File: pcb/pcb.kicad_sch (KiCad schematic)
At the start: 247 parts, among them J1 USB_C_Receptacle_USB2.0, J2 AVR-ISP-6, SW1 1U, SW10 1U, SW100 2U, SW101 1.25U CTRL, SW102 1.25U GUI, SW103 1.25U ALT, SW104 6.25u SPACE, SW105 1U ALT, SW106 1U GUI, SW107 1U CTRL, SW108 1U, SW109 1U, SW11 1U, SW110 1U, SW111 1U, SW112 1U, SW113 1U, SW114 1.5U CTRL, SW115 1U GUI, SW116 1.5U ALT, SW117 7U SPACE, SW118 1.5U ALT, SW119 1.5U CTRL, SW12 1U, SW120 1.5U GUI, SW121 6U SPACE, SW122 SW_Push, SW123 SW_Push, SW13 1U, SW14 1U, SW15 1U, SW16 1U, SW17 1U, SW18 1U, SW19 1U, SW2 1U, SW20 1U, SW21 1U, SW22 1U, SW23 1U, SW24 1U, SW25 1U, SW26 1U, SW27 1U, SW28 1U, SW29 1U, SW3 1U, SW30 1U, SW31 1U, SW32 1U, SW33 1U, SW34 1U, SW35 1U, SW36 1U, SW37 1U, SW38 1U, SW39 1U, SW4 1U, SW40 1U, SW41 2U, SW42 1U, SW43 1.5U, SW44 1U, SW45 1U, SW46 1U, SW47 1U, SW48 1U, SW49 1U, SW5 1U, SW50 1U, SW51 1U, SW52 1U, SW53 1U, SW54 1U, SW55 1.5U, SW56 1U, SW57 1U, SW58 1U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

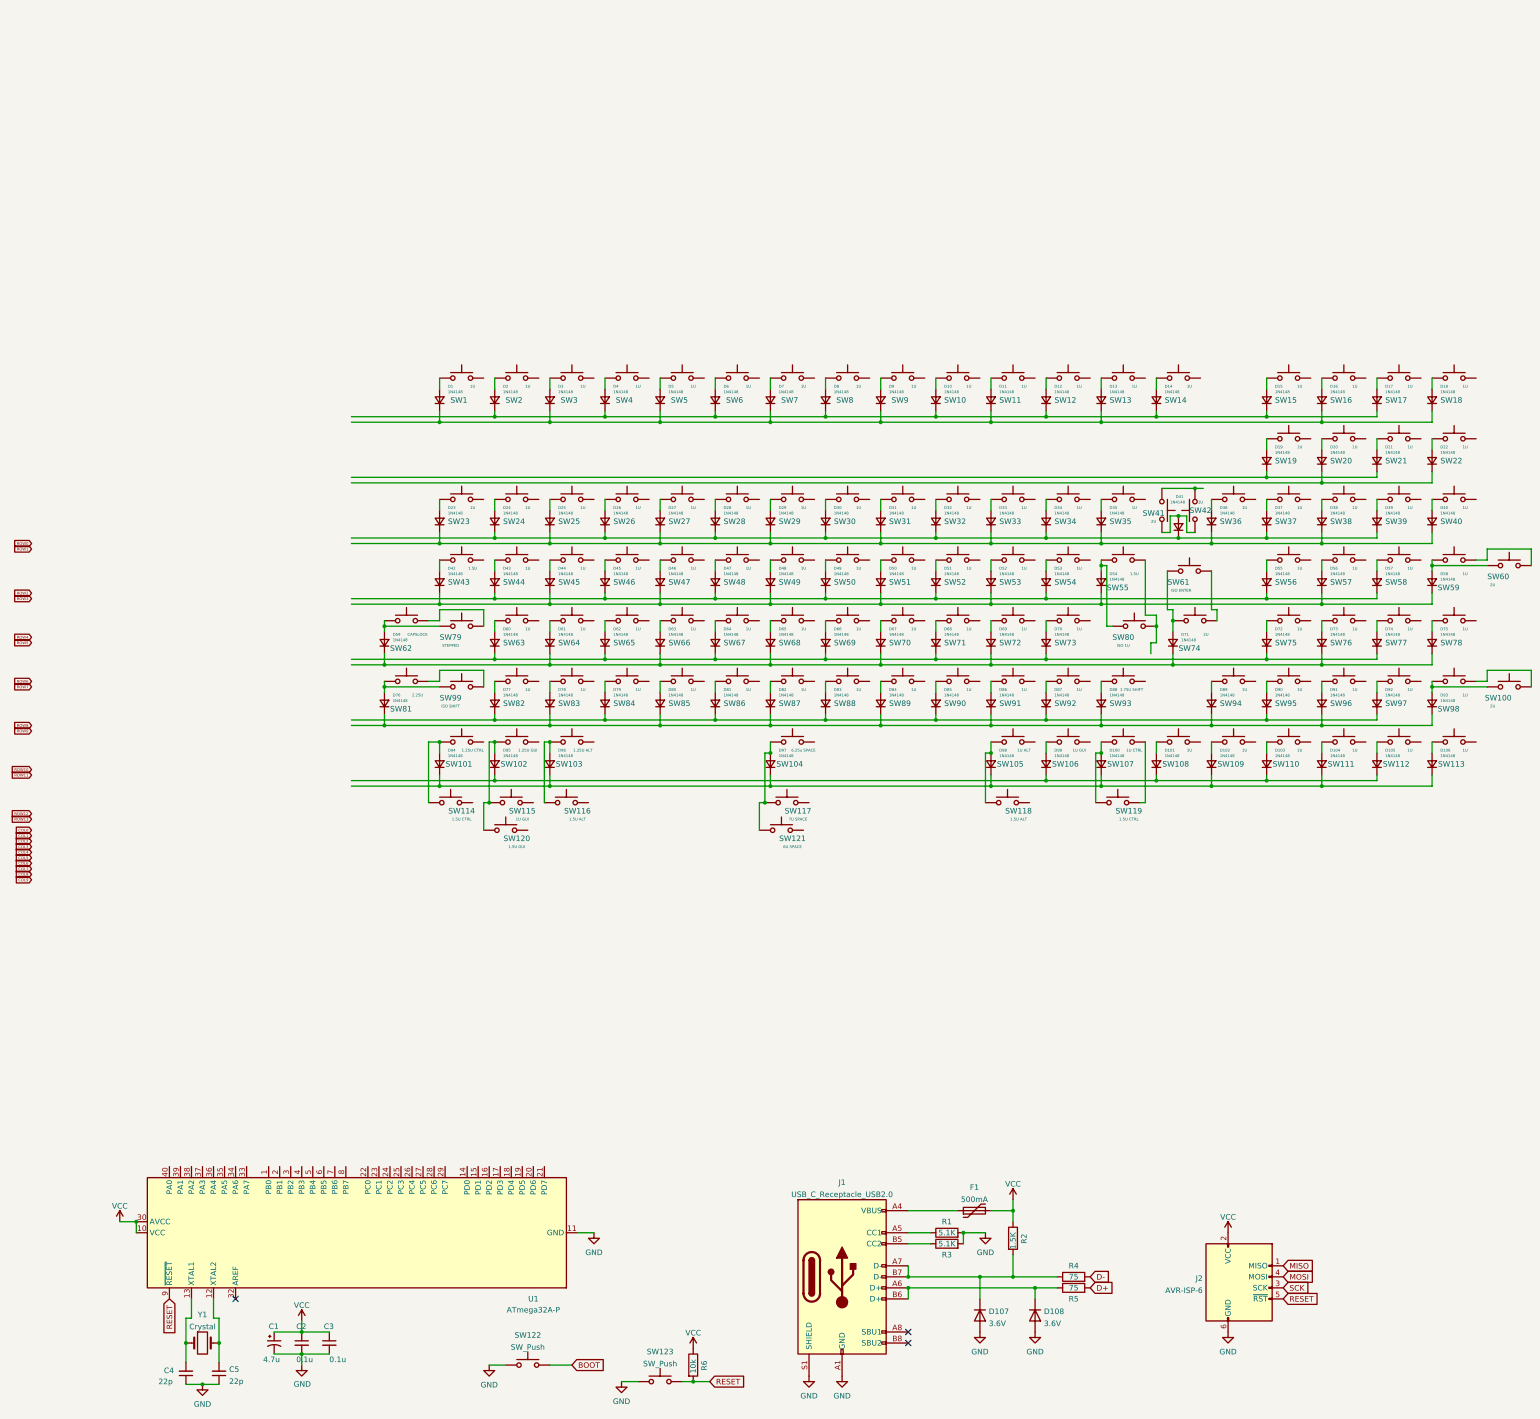
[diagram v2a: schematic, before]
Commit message: Main wiring schematic finally done, keys organized on PCB
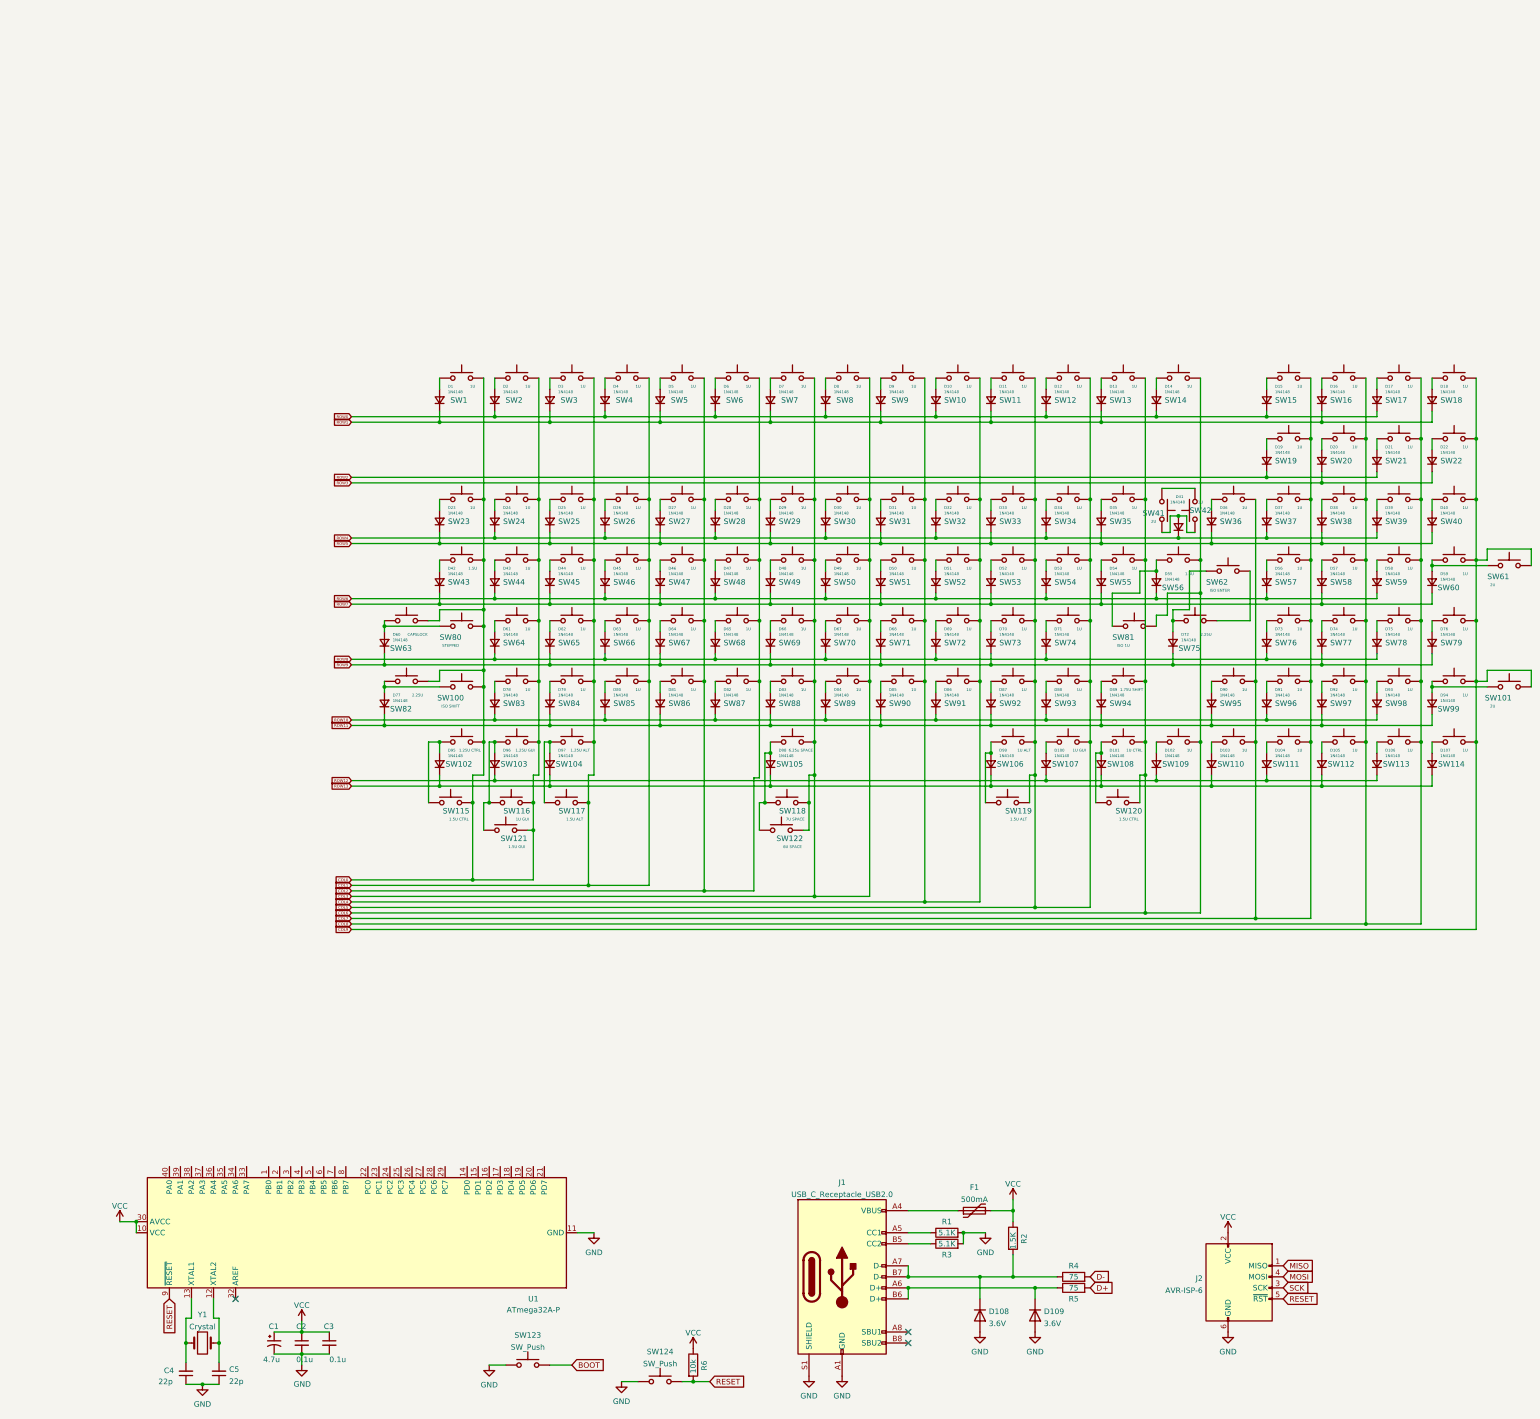
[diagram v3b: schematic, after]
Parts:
- added D54: 1N4148, Diode_THT:D_DO-35_SOD27_P7.62mm_Horizontal, symbol Device:D_Small
- added SW55: 1U, MX_Only:MXOnly-1U-NoLED, symbol Switch:SW_Push
- SW101: renamed from SW100; footprint MX_Only:MXOnly-2U-NoLED -> MX_Only:MXOnly-2U-VerticalStabilizers-NoLED
- SW61: renamed from SW60; footprint MX_Only:MXOnly-2U-NoLED -> MX_Only:MXOnly-2U-VerticalStabilizers-NoLED
- SW75: renamed from SW74; value 2U -> 2.25U; footprint MX_Only:MXOnly-2U-NoLED -> MX_Only:MXOnly-2.25U-NoLED
- renumbered D99 to D100, D100 to D101, D101 to D102, D102 to D103, D103 to D104, D104 to D105, D105 to D106, D106 to D107, D107 to D108, D108 to D109, D54 to D55, D55 to D56, D56 to D57, D57 to D58, D58 to D59, D59 to D60, D60 to D61, D61 to D62, D62 to D63, D63 to D64, D64 to D65, D65 to D66, D66 to D67, D67 to D68, D68 to D69, D69 to D70, D70 to D71, D71 to D72, D72 to D73, D73 to D74, D74 to D75, D75 to D76, D76 to D77, D77 to D78, D78 to D79, D79 to D80, D80 to D81, D81 to D82, D82 to D83, D83 to D84, D84 to D85, D85 to D86, D86 to D87, D87 to D88, D88 to D89, D89 to D90, D90 to D91, D91 to D92, D92 to D93, D93 to D94, D94 to D95, D95 to D96, D96 to D97, D97 to D98, D98 to D99, SW99 to SW100, SW101 to SW102, SW102 to SW103, SW103 to SW104, SW104 to SW105, SW105 to SW106, SW106 to SW107, SW107 to SW108, SW108 to SW109, SW109 to SW110, SW110 to SW111, SW111 to SW112, SW112 to SW113, SW113 to SW114, SW114 to SW115, SW115 to SW116, SW116 to SW117, SW117 to SW118, SW118 to SW119, SW119 to SW120, SW120 to SW121, SW121 to SW122, SW122 to SW123, SW123 to SW124, SW55 to SW56, SW56 to SW57, SW57 to SW58, SW58 to SW59, SW59 to SW60, SW61 to SW62, SW62 to SW63, SW63 to SW64, SW64 to SW65, SW65 to SW66, SW66 to SW67, SW67 to SW68, SW68 to SW69, SW69 to SW70, SW70 to SW71, SW71 to SW72, SW72 to SW73, SW73 to SW74, SW75 to SW76, SW76 to SW77, SW77 to SW78, SW78 to SW79, SW79 to SW80, SW80 to SW81, SW81 to SW82, SW82 to SW83, SW83 to SW84, SW84 to SW85, SW85 to SW86, SW86 to SW87, SW87 to SW88, SW88 to SW89, SW89 to SW90, SW90 to SW91, SW91 to SW92, SW92 to SW93, SW93 to SW94, SW94 to SW95, SW95 to SW96, SW96 to SW97, SW97 to SW98, SW98 to SW99
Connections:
- net COL0: now also SW1.2, SW100.2, SW102.2, SW103.2, SW115.2, SW116.2, SW121.2, SW2.2, SW23.2, SW24.2, SW43.2, SW44.2, SW63.2, SW64.2, SW80.2, SW82.2, SW83.2
- net COL1: now also SW104.2, SW117.2, SW25.2, SW26.2, SW3.2, SW4.2, SW45.2, SW46.2, SW65.2, SW66.2, SW84.2, SW85.2
- net COL2: now also SW27.2, SW28.2, SW47.2, SW48.2, SW5.2, SW6.2, SW67.2, SW68.2, SW86.2, SW87.2
- net COL3: now also SW105.2, SW118.2, SW122.2, SW29.2, SW30.2, SW49.2, SW50.2, SW69.2, SW7.2, SW70.2, SW8.2, SW88.2, SW89.2
- net COL4: now also SW10.2, SW31.2, SW32.2, SW51.2, SW52.2, SW71.2, SW72.2, SW9.2, SW90.2, SW91.2
- net COL5: now also SW106.2, SW107.2, SW11.2, SW119.2, SW12.2, SW33.2, SW34.2, SW53.2, SW54.2, SW73.2, SW74.2, SW92.2, SW93.2
- net COL6: now also SW108.2, SW109.2, SW120.2, SW13.2, SW14.2, SW35.2, SW56.2, SW81.2, SW94.2, SW55.2
- net COL7: now also SW110.2, SW111.2, SW15.2, SW19.2, SW36.2, SW37.2, SW57.2, SW76.2, SW95.2, SW96.2
- net COL8: now also SW112.2, SW113.2, SW16.2, SW17.2, SW20.2, SW21.2, SW38.2, SW39.2, SW58.2, SW59.2, SW77.2, SW78.2, SW97.2, SW98.2
- net COL9: now also SW101.2, SW114.2, SW18.2, SW22.2, SW40.2, SW60.2, SW61.2, SW79.2, SW99.2
- net ROW0: now also D10.1 (K), D12.1 (K), D14.1 (K), D15.1 (K), D17.1 (K), D2.1 (K), D4.1 (K), D6.1 (K), D8.1 (K)
- net ROW1: now also D1.1 (K), D11.1 (K), D13.1 (K), D16.1 (K), D18.1 (K), D3.1 (K), D5.1 (K), D7.1 (K), D9.1 (K)
- net ROW10: now also D78.1 (K), D80.1 (K), D82.1 (K), D84.1 (K), D86.1 (K), D88.1 (K), D91.1 (K), D93.1 (K)
- net ROW11: now also D77.1 (K), D79.1 (K), D81.1 (K), D83.1 (K), D85.1 (K), D87.1 (K), D89.1 (K), D90.1 (K), D92.1 (K), D94.1 (K)
- net ROW12: now also D100.1 (K), D102.1 (K), D104.1 (K), D106.1 (K), D96.1 (K)
- net ROW13: now also D101.1 (K), D103.1 (K), D105.1 (K), D107.1 (K), D95.1 (K), D97.1 (K), D98.1 (K), D99.1 (K)
- net ROW2: now also D19.1 (K), D21.1 (K)
- net ROW3: now also D20.1 (K), D22.1 (K)
- net ROW4: now also D24.1 (K), D26.1 (K), D28.1 (K), D30.1 (K), D32.1 (K), D34.1 (K), D37.1 (K), D39.1 (K), D41.1 (K)
- net ROW5: now also D23.1 (K), D25.1 (K), D27.1 (K), D29.1 (K), D31.1 (K), D33.1 (K), D35.1 (K), D36.1 (K), D38.1 (K), D40.1 (K)
- net ROW6: now also D43.1 (K), D45.1 (K), D47.1 (K), D49.1 (K), D51.1 (K), D53.1 (K), D55.1 (K), D56.1 (K), D58.1 (K)
- net ROW7: now also D42.1 (K), D44.1 (K), D46.1 (K), D48.1 (K), D50.1 (K), D52.1 (K), D57.1 (K), D59.1 (K), D54.1 (K)
- net ROW8: now also D61.1 (K), D63.1 (K), D65.1 (K), D67.1 (K), D69.1 (K), D71.1 (K), D73.1 (K), D75.1 (K)
- net ROW9: now also D60.1 (K), D62.1 (K), D64.1 (K), D66.1 (K), D68.1 (K), D70.1 (K), D72.1 (K), D74.1 (K), D76.1 (K)
- new net: D54.2 (A), SW55.1
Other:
- moved on the sheet: D55, SW56, SW62

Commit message: PCB components placed
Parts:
- removed D41: 1N4148, Diode_THT:D_DO-35_SOD27_P7.62mm_Horizontal, symbol Device:D_Small
- removed SW41: 2U, MX_Only:MXOnly-2U-NoLED, symbol Switch:SW_Push
- removed SW42: 1U, MX_Only:MXOnly-1U-NoLED, symbol Switch:SW_Push
- added D36: 1N4148, Diode_THT:D_DO-35_SOD27_P7.62mm_Horizontal, symbol Device:D_Small
- added SW23: 1U, MX_Only:MXOnly-1U-NoLED, symbol Switch:SW_Push
- added SW37: 2U, MX_Only:MXOnly-2U-NoLED, symbol Switch:SW_Push
- renumbered D36 to D37, D37 to D38, D38 to D39, D39 to D40, D40 to D41, SW23 to SW24, SW24 to SW25, SW25 to SW26, SW26 to SW27, SW27 to SW28, SW28 to SW29, SW29 to SW30, SW30 to SW31, SW31 to SW32, SW32 to SW33, SW33 to SW34, SW34 to SW35, SW35 to SW36, SW36 to SW38, SW37 to SW39, SW38 to SW40, SW39 to SW41, SW40 to SW42
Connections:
- net COL6: now also SW62.2, SW75.2, SW23.2, SW37.2
- net ROW4: now also D36.1 (K)
- new net: D36.2 (A), SW23.1, SW37.1

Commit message: God help me with these diodes
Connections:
- net ROW13 is gone; now on net ROW12: D101.1 (K), D103.1 (K), D105.1 (K), D107.1 (K), D95.1 (K), D97.1 (K), D98.1 (K), D99.1 (K)
- net COL0: now also U1.28 (PC6)
- net COL1: now also U1.29 (PC7)
- net COL2: now also U1.33 (PA7)
- net COL3: now also U1.34 (PA6)
- net COL4: now also U1.35 (PA5)
- net COL5: now also U1.36 (PA4)
- net COL6: now also U1.37 (PA3)
- net COL7: now also U1.38 (PA2)
- net COL8: now also U1.39 (PA1)
- net COL9: now also U1.40 (PA0)
- net D+: now also U1.26 (PC4)
- net D-: now also U1.27 (PC5)
- net MISO: now also U1.15 (PD1)
- net MOSI: now also U1.16 (PD2)
- net ROW10: now also D77.1 (K), D79.1 (K), D81.1 (K), D83.1 (K), D85.1 (K), D87.1 (K), D89.1 (K), D90.1 (K), D92.1 (K), D94.1 (K); no longer D78.1 (K), D80.1 (K), D82.1 (K), D84.1 (K), D86.1 (K), D88.1 (K), D91.1 (K), D93.1 (K)
- net ROW11: now also D100.1 (K), D102.1 (K), D104.1 (K), D106.1 (K), D96.1 (K); no longer D77.1 (K), D79.1 (K), D81.1 (K), D83.1 (K), D85.1 (K), D87.1 (K), D89.1 (K), D90.1 (K), D92.1 (K), D94.1 (K)
- net ROW12: no longer D100.1 (K), D102.1 (K), D104.1 (K), D106.1 (K), D96.1 (K)
- net ROW2: now also D20.1 (K), D22.1 (K)
- net ROW3: now also D24.1 (K), D26.1 (K), D28.1 (K), D30.1 (K), D32.1 (K), D34.1 (K), D36.1 (K), D38.1 (K), D40.1 (K); no longer D20.1 (K), D22.1 (K)
- net ROW4: now also D23.1 (K), D25.1 (K), D27.1 (K), D29.1 (K), D31.1 (K), D33.1 (K), D35.1 (K), D37.1 (K), D39.1 (K), D41.1 (K); no longer D24.1 (K), D26.1 (K), D28.1 (K), D30.1 (K), D32.1 (K), D34.1 (K), D36.1 (K), D38.1 (K), D40.1 (K)
- net ROW5: now also D43.1 (K), D45.1 (K), D47.1 (K), D49.1 (K), D51.1 (K), D53.1 (K), D55.1 (K), D56.1 (K), D58.1 (K); no longer D23.1 (K), D25.1 (K), D27.1 (K), D29.1 (K), D31.1 (K), D33.1 (K), D35.1 (K), D37.1 (K), D39.1 (K), D41.1 (K)
- net ROW6: now also D42.1 (K), D44.1 (K), D46.1 (K), D48.1 (K), D50.1 (K), D52.1 (K), D54.1 (K), D57.1 (K), D59.1 (K); no longer D43.1 (K), D45.1 (K), D47.1 (K), D49.1 (K), D51.1 (K), D53.1 (K), D55.1 (K), D56.1 (K), D58.1 (K)
- net ROW7: now also D61.1 (K), D63.1 (K), D65.1 (K), D67.1 (K), D69.1 (K), D71.1 (K), D73.1 (K), D75.1 (K); no longer D42.1 (K), D44.1 (K), D46.1 (K), D48.1 (K), D50.1 (K), D52.1 (K), D54.1 (K), D57.1 (K), D59.1 (K)
- net ROW8: now also D60.1 (K), D62.1 (K), D64.1 (K), D66.1 (K), D68.1 (K), D70.1 (K), D72.1 (K), D74.1 (K), D76.1 (K); no longer D61.1 (K), D63.1 (K), D65.1 (K), D67.1 (K), D69.1 (K), D71.1 (K), D73.1 (K), D75.1 (K)
- net ROW9: now also D78.1 (K), D80.1 (K), D82.1 (K), D84.1 (K), D86.1 (K), D88.1 (K), D91.1 (K), D93.1 (K); no longer D60.1 (K), D62.1 (K), D64.1 (K), D66.1 (K), D68.1 (K), D70.1 (K), D72.1 (K), D74.1 (K), D76.1 (K)
- net SCK: now also U1.14 (PD0)

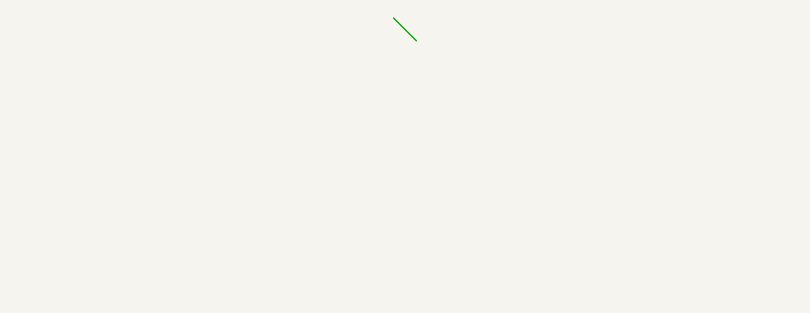
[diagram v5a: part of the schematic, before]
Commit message: Started routing of rows
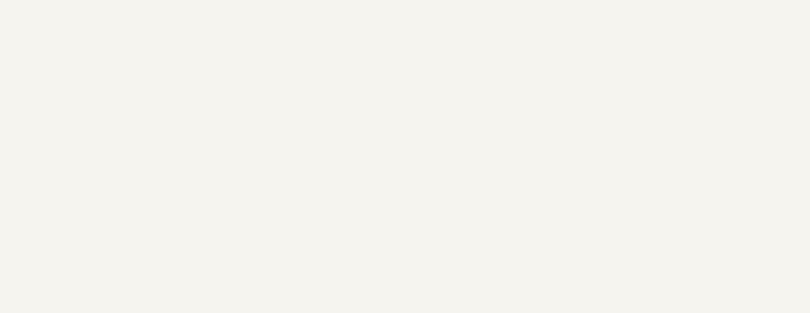
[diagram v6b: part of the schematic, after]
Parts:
- SW101, SW61: footprint MX_Only:MXOnly-2U-VerticalStabilizers-NoLED -> MX_Only:MXOnly-2U-ReversedVerticalStabilizers-NoLED
- SW105: footprint MX_Only:MXOnly-6.25U-NoLED -> MX_Only:MXOnly-6.25U-ReversedStabilizers-NoLED
- SW118: footprint MX_Only:MXOnly-7U-NoLED -> MX_Only:MXOnly-7U-ReversedStabilizers-NoLED
- SW122: footprint MX_Only:MXOnly-6U-NoLED -> MX_Only:MXOnly-6U-ReversedStabilizers-NoLED
- SW62: footprint MX_Only:MXOnly-ISO-NoLED -> MX_Only:MXOnly-ISO-ReversedStabilizers-NoLED
- SW75, SW82: footprint MX_Only:MXOnly-2.25U-NoLED -> MX_Only:MXOnly-2.25U-ReversedStabilizers-NoLED
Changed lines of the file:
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@@
   (no_connect (at 45.72 255.27))
   (no_connect (at 200.66 262.89))
-  (bus_entry (at 207.645 -41.91) (size 2.54 2.54)
-    (stroke (width 0) (type default) (color 0 0 0 0))
-  )
   (wire (pts (xy 232.41 52.07) (xy 257.81 52.07))
     (stroke (width 0) (type default) (color 0 0 0 0))
@@
       (effects (font (size 0.635 0.635)))
     )
-    (property "Footprint" "MX_Only:MXOnly-2U-VerticalStabilizers-NoLED" (id 2) (at 339.09 109.22 0)
+    (property "Footprint" "MX_Only:MXOnly-2U-ReversedVerticalStabilizers-NoLED" (id 2) (at 339.09 109.22 0)
       (effects (font (size 1.27 1.27)) hide)
     )
@@
       (effects (font (size 0.635 0.635)))
     )
-    (property "Footprint" "MX_Only:MXOnly-ISO-NoLED" (id 2) (at 274.32 82.55 0)
+    (property "Footprint" "MX_Only:MXOnly-ISO-ReversedStabilizers-NoLED" (id 2) (at 274.32 82.55 0)
       (effects (font (size 1.27 1.27)) hide)
     )
@@
       (effects (font (size 0.635 0.635)))
     )
-    (property "Footprint" "MX_Only:MXOnly-2.25U-NoLED" (id 2) (at 266.7 93.98 0)
+    (property "Footprint" "MX_Only:MXOnly-2.25U-ReversedStabilizers-NoLED" (id 2) (at 266.7 93.98 0)
       (effects (font (size 1.27 1.27)) hide)
     )
@@
       (effects (font (size 0.635 0.635)))
     )
-    (property "Footprint" "MX_Only:MXOnly-2.25U-NoLED" (id 2) (at 85.09 107.95 0)
+    (property "Footprint" "MX_Only:MXOnly-2.25U-ReversedStabilizers-NoLED" (id 2) (at 85.09 107.95 0)
       (effects (font (size 1.27 1.27)) hide)
     )
@@
       (effects (font (size 0.635 0.635)))
     )
-    (property "Footprint" "MX_Only:MXOnly-2U-VerticalStabilizers-NoLED" (id 2) (at 339.09 81.28 0)
+    (property "Footprint" "MX_Only:MXOnly-2U-ReversedVerticalStabilizers-NoLED" (id 2) (at 339.09 81.28 0)
       (effects (font (size 1.27 1.27)) hide)
     )
@@
       (effects (font (size 0.635 0.635)))
     )
-    (property "Footprint" "MX_Only:MXOnly-6U-NoLED" (id 2) (at 171.45 142.24 0)
+    (property "Footprint" "MX_Only:MXOnly-6U-ReversedStabilizers-NoLED" (id 2) (at 171.45 142.24 0)
       (effects (font (size 1.27 1.27)) hide)
     )
@@
       (effects (font (size 0.635 0.635)))
     )
-    (property "Footprint" "MX_Only:MXOnly-6.25U-NoLED" (id 2) (at 173.99 121.92 0)
+    (property "Footprint" "MX_Only:MXOnly-6.25U-ReversedStabilizers-NoLED" (id 2) (at 173.99 121.92 0)
       (effects (font (size 1.27 1.27)) hide)
     )
@@
       (effects (font (size 0.635 0.635)))
     )
-    (property "Footprint" "MX_Only:MXOnly-7U-NoLED" (id 2) (at 172.72 135.89 0)
+    (property "Footprint" "MX_Only:MXOnly-7U-ReversedStabilizers-NoLED" (id 2) (at 172.72 135.89 0)
       (effects (font (size 1.27 1.27)) hide)
     )
@@
     )
     (path "/2b191c2c-1167-46dd-8fa0-bd72c7ca26a5"
-      (reference "SW61") (unit 1) (value "2U") (footprint "MX_Only:MXOnly-2U-VerticalStabilizers-NoLED")
+      (reference "SW61") (unit 1) (value "2U") (footprint "MX_Only:MXOnly-2U-ReversedVerticalStabilizers-NoLED")
     )
     (path "/0a230cfb-8793-470f-a80a-242a8a103a1d"
-      (reference "SW62") (unit 1) (value "ISO ENTER") (footprint "MX_Only:MXOnly-ISO-NoLED")
+      (reference "SW62") (unit 1) (value "ISO ENTER") (footprint "MX_Only:MXOnly-ISO-ReversedStabilizers-NoLED")
     )
     (path "/1bff9b0c-815d-4638-9245-2e23157e575b"
@@
     )
     (path "/140f8e65-10c9-4167-a031-edff93ac62c5"
-      (reference "SW75") (unit 1) (value "2.25U") (footprint "MX_Only:MXOnly-2.25U-NoLED")
+      (reference "SW75") (unit 1) (value "2.25U") (footprint "MX_Only:MXOnly-2.25U-ReversedStabilizers-NoLED")
     )
     (path "/1c59a2fc-2e4a-4038-8c07-08e6e2cee30d"
@@
     )
     (path "/234835dd-0a94-4a66-ba5a-63df4a898804"
-      (reference "SW82") (unit 1) (value "2.25U") (footprint "MX_Only:MXOnly-2.25U-NoLED")
+      (reference "SW82") (unit 1) (value "2.25U") (footprint "MX_Only:MXOnly-2.25U-ReversedStabilizers-NoLED")
     )
     (path "/b9f2f4af-d52e-46dc-a152-d7e3d3b385f7"
@@
     )
     (path "/03681980-a6c5-4231-b7d5-b4a4c9252c6e"
-      (reference "SW101") (unit 1) (value "2U") (footprint "MX_Only:MXOnly-2U-VerticalStabilizers-NoLED")
+      (reference "SW101") (unit 1) (value "2U") (footprint "MX_Only:MXOnly-2U-ReversedVerticalStabilizers-NoLED")
     )
     (path "/544d55a0-6b4c-4ad8-81fd-694d0fa9dace"
@@
     )
     (path "/63485bc8-3e20-4245-9f8d-3d159167a3f2"
-      (reference "SW105") (unit 1) (value "6.25u SPACE") (footprint "MX_Only:MXOnly-6.25U-NoLED")
+      (reference "SW105") (unit 1) (value "6.25u SPACE") (footprint "MX_Only:MXOnly-6.25U-ReversedStabilizers-NoLED")
     )
     (path "/be2727b2-cae7-4411-8bf6-0e1007259dbb"
@@
     )
     (path "/dcb31f0c-7e8f-4c36-97ce-35aab54b5477"
-      (reference "SW118") (unit 1) (value "7U SPACE") (footprint "MX_Only:MXOnly-7U-NoLED")
+      (reference "SW118") (unit 1) (value "7U SPACE") (footprint "MX_Only:MXOnly-7U-ReversedStabilizers-NoLED")
     )
     (path "/d2d4d20d-7cac-43ba-a941-57dd1c25ddb5"
@@
     )
     (path "/3d5d0f67-24dd-4ec0-a75c-164b57b95844"
-      (reference "SW122") (unit 1) (value "6U SPACE") (footprint "MX_Only:MXOnly-6U-NoLED")
+      (reference "SW122") (unit 1) (value "6U SPACE") (footprint "MX_Only:MXOnly-6U-ReversedStabilizers-NoLED")
     )
     (path "/fabae21c-0bf5-41e1-92c8-b0440c8cdf3c"
